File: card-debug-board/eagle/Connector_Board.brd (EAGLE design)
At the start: 69.9 x 34.3 mm, 32 parts, among them J1 ORESAT-DEBUG-CONNECTOR-CARD, J3 USB_A_SMT_FEMALE, Q1 MOSFET-PCH-SOT23-6, U1 FT230XS-R

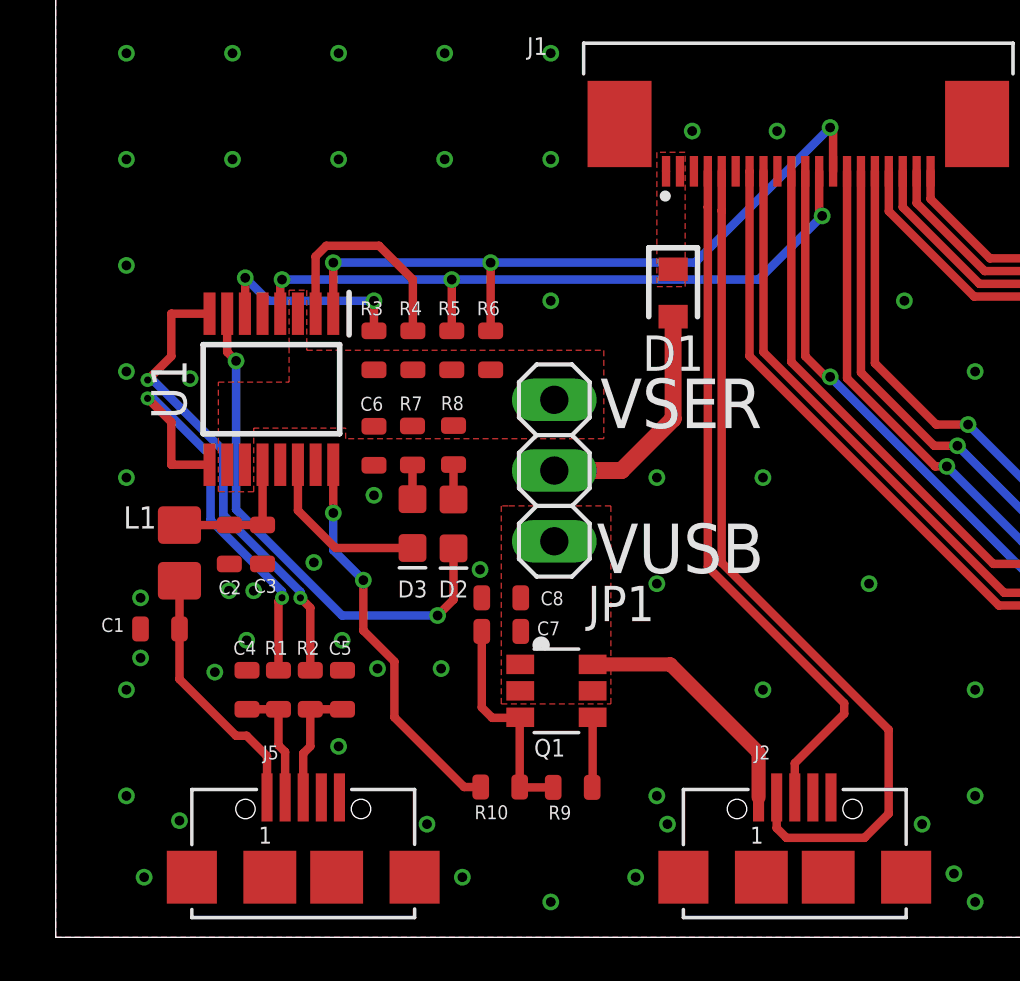
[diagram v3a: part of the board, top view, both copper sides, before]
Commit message: Clear stubs and DRC errors
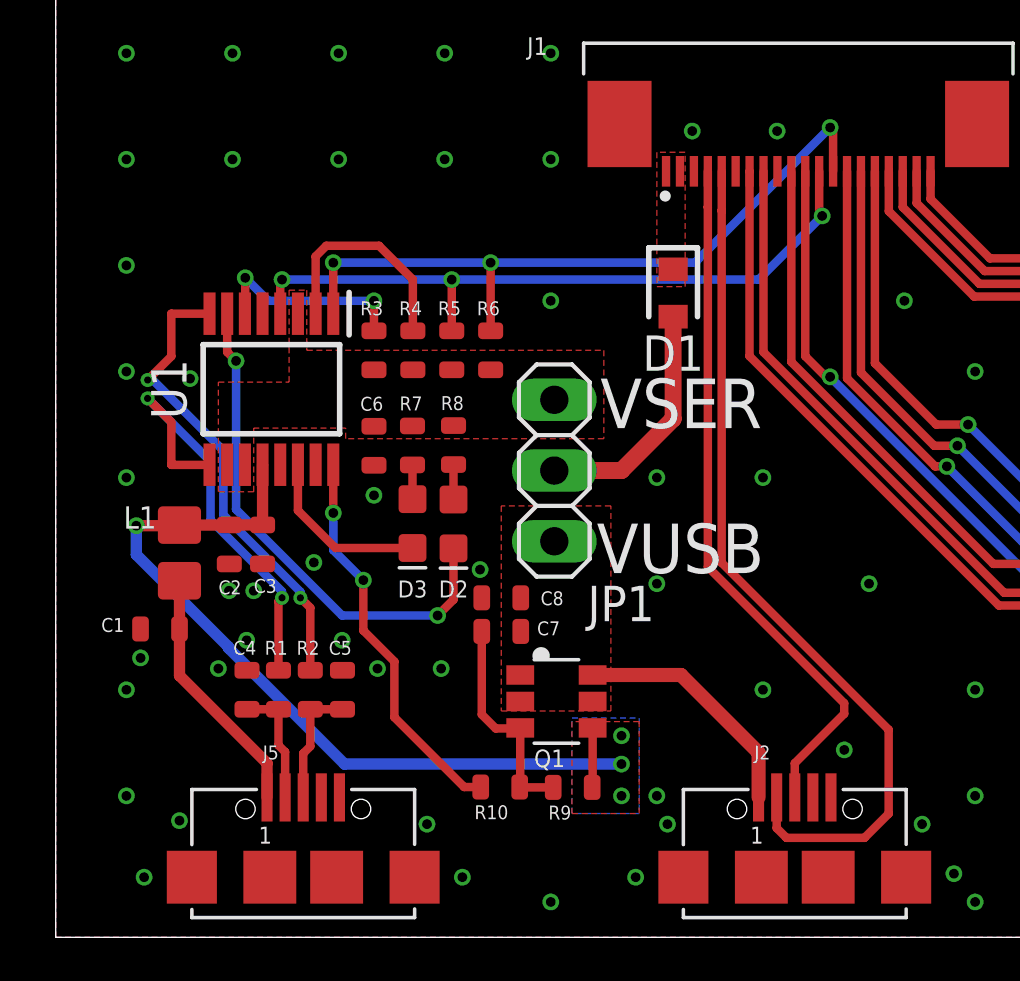
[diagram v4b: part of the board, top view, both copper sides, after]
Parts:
- moved Q1 0.38 mm to (18.0, 8.47)
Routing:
- net VCC: track 7.68 -> 30.5 mm, vias 0 -> 4
- added copper zone on layer 1, net VCC
- added copper zone on layer 16, net VCC

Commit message: clear all ERC errors
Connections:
- removed net GND_2: U1.13
- net GND: now also U1.13
